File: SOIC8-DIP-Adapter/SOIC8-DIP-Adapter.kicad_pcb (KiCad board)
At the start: 2 copper layers, 13 x 10 mm, 3 parts, among them J1 01-04, J2 05-08, U1 SOIC-8

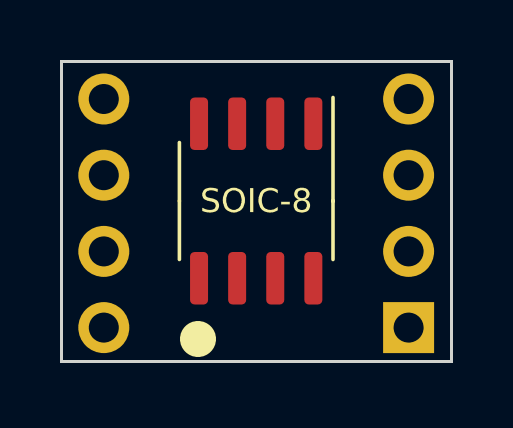
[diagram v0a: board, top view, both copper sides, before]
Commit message: Finish SOIC-8 adapter
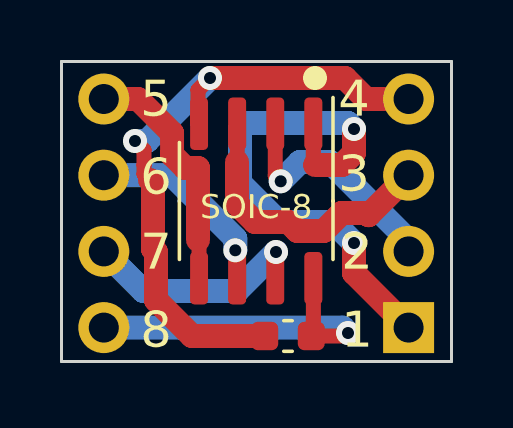
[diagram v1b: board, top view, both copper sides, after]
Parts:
- added C1: C_Small, Capacitor_SMD:C_0603_1608Metric, F.Cu at (143.3, 93.4)
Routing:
- net Net-(J1-Pad4): track 0.00 -> 21.6 mm, vias 0 -> 2
- net Net-(J1-Pad1): track 0.00 -> 17.6 mm, vias 0 -> 2
- net Net-(J2-Pad4): track 0.00 -> 11.4 mm, vias 0 -> 1
- net Net-(J1-Pad3): track 0.00 -> 9.60 mm
- net Net-(J2-Pad1): track 0.00 -> 8.21 mm
- net Net-(J1-Pad2): track 0.00 -> 7.97 mm, vias 0 -> 1
- net Net-(J2-Pad3): track 0.00 -> 7.71 mm, vias 0 -> 1
- net Net-(J2-Pad2): track 0.00 -> 6.61 mm, vias 0 -> 1
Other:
- board text added: "1"
- board text added: "2"
- board text added: "3"
- board text added: "4"
- board text added: "5"
- board text added: "6"
- board text added: "7"
- board text added: "8"
